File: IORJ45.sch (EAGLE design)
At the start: 19 parts, among them J3 RJ45-8X44UCON19514

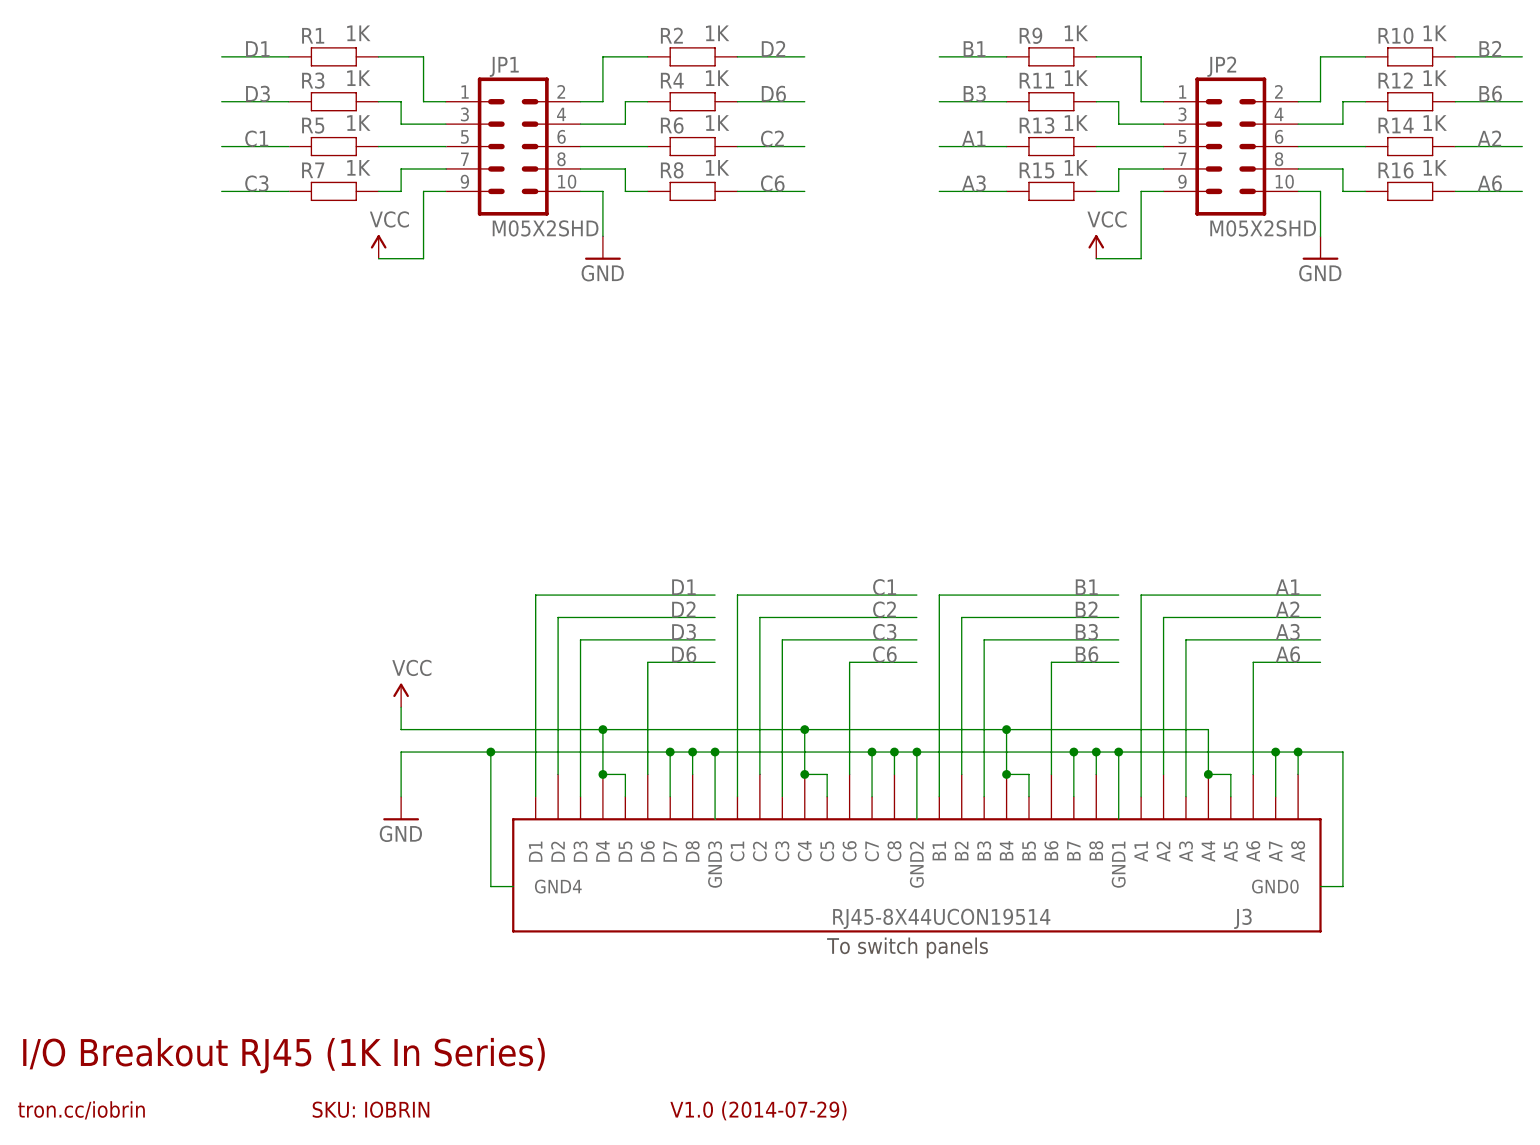
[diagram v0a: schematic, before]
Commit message: Converted to 2x6 header for v2.0 release
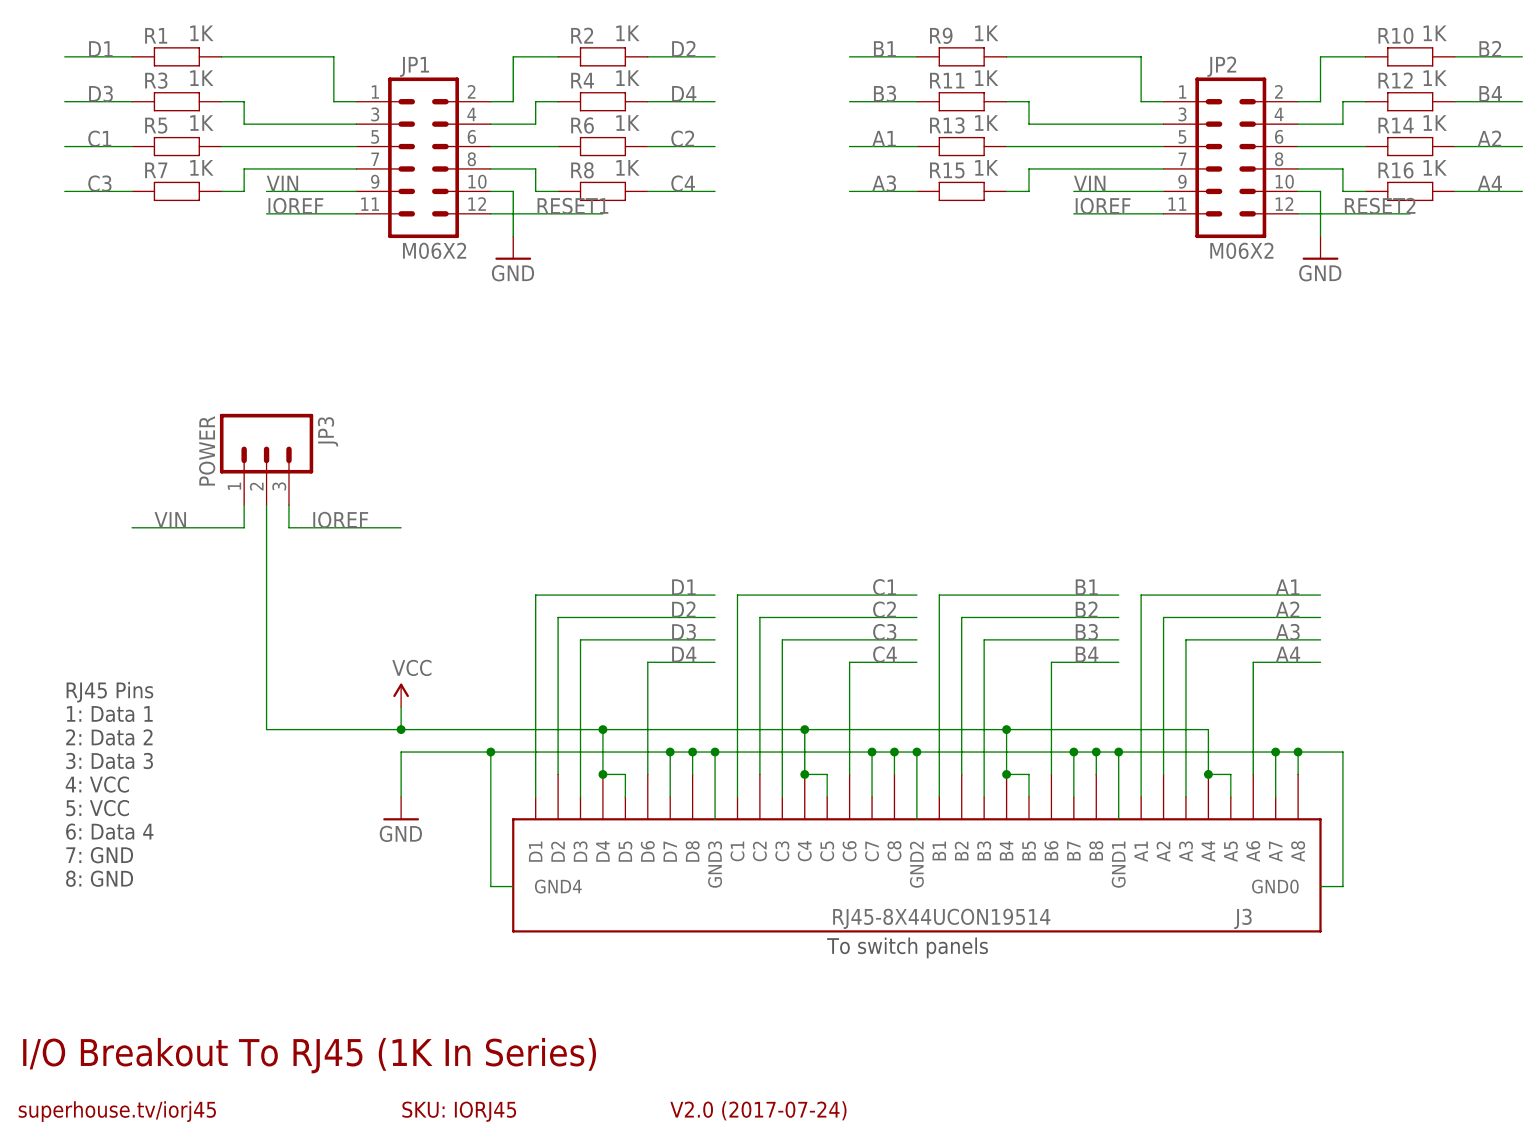
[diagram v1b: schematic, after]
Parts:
- added JP3: POWER, freetronics-jon:M03PTH
- J3: device freetronics-2:RJ45-8X44UCON19514 -> freetronics-jon:RJ45-8X44UCON19514
- JP1, JP2: value M05X2SHD -> M06X2; device freetronics-original:M05X2SHD -> freetronics-jon:M06X2
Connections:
- net A6 renamed A4
- net B6 renamed B4
- net C6 renamed C4
- net D6 renamed D4
- new net IOREF: JP1.11, JP2.11, JP3.3
- new net RESET1: JP1.12
- new net RESET2: JP2.12
- new net VIN: JP1.9, JP2.9, JP3.1
- net VCC: now also JP3.2; no longer JP1.9, JP2.9
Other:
- note added: "I/O Breakout To RJ45 (1K In Series)"
- note added: "RJ45 Pins 1: Data 1 2: Data 2 3: Data 3 4: VCC 5: VCC 6: Data 4 7: GND 8: GND"
- note added: "SKU: IORJ45"
- note added: "V2.0 (2017-07-24)"
- note added: "superhouse.tv/iorj45"
- note removed: "I/O Breakout RJ45 (1K In Series)"
- note removed: "SKU: IOBRIN"
- note removed: "V1.0 (2014-07-29)"
- note removed: "tron.cc/iobrin"
- moved on the sheet: R1, R11, R13, R15, R2, R3, R4, R5, R6, R7, R8, R9

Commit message: Part replacement using SuperHouse libraries
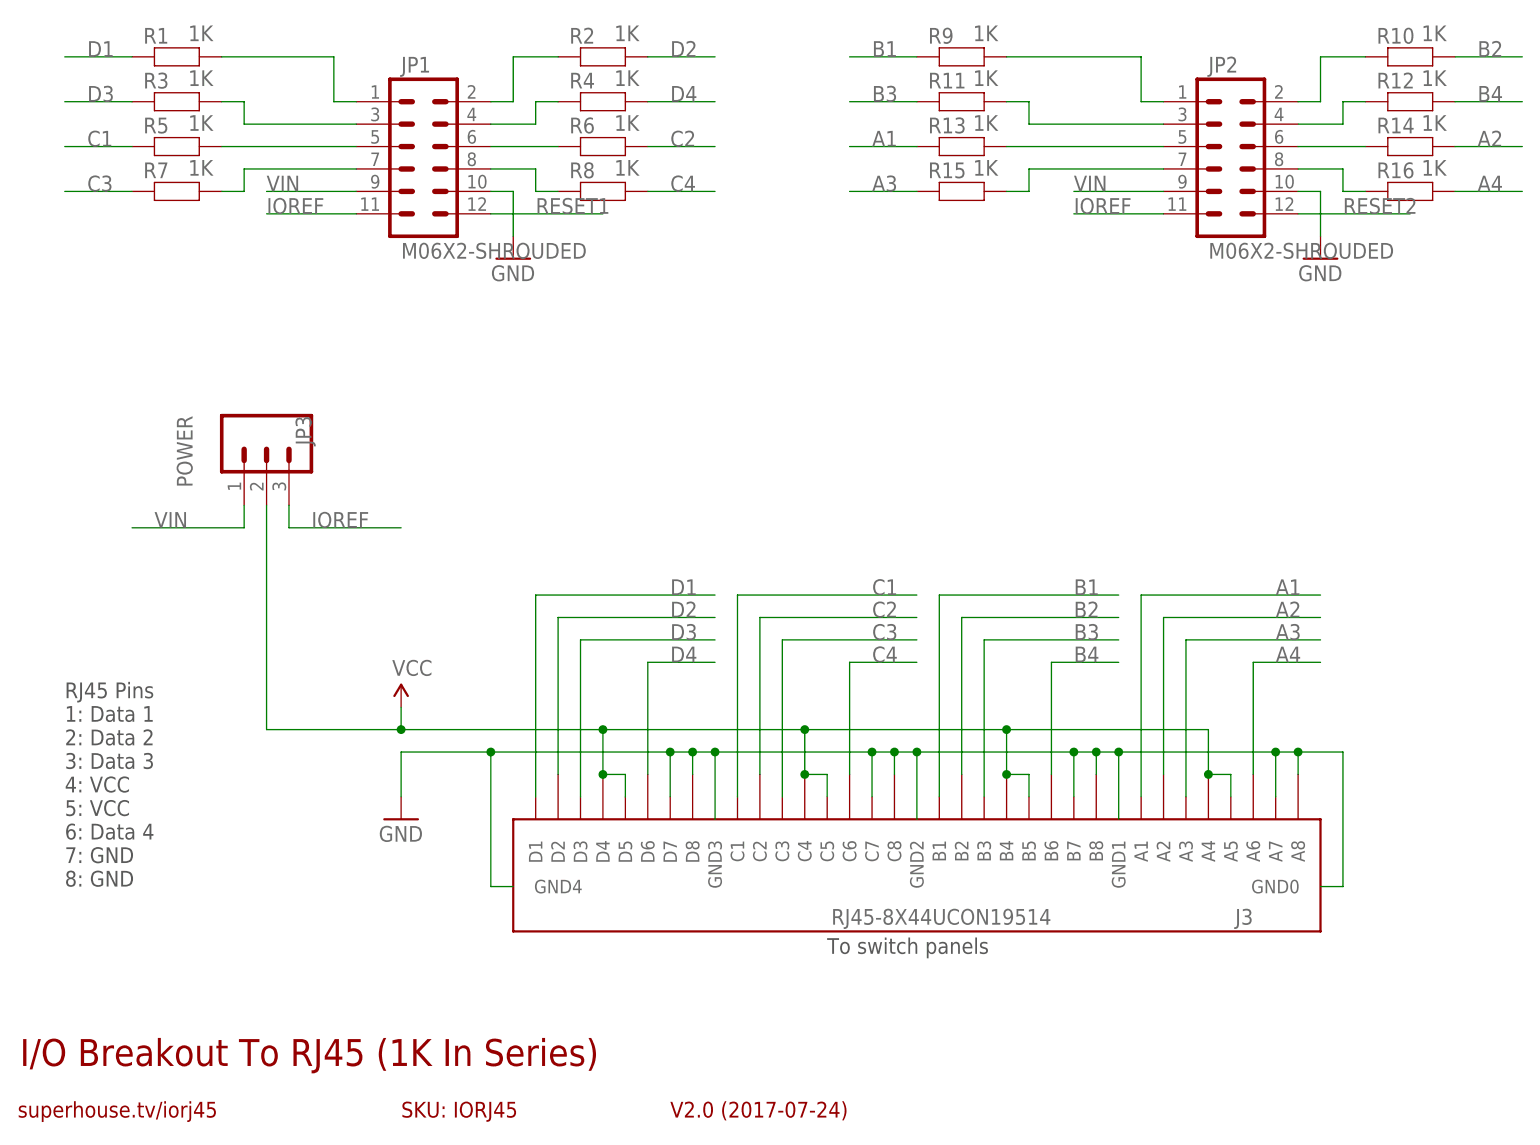
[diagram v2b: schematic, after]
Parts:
- J3: device freetronics-jon:RJ45-8X44UCON19514 -> SuperHouse-Connectors:RJ45-8X44UCON19514
- JP1, JP2: value M06X2 -> M06X2-SHROUDED; device freetronics-jon:M06X2 -> SuperHouse-Connectors:M06X2-SHROUDED
- JP3: device freetronics-jon:M03PTH -> SuperHouse-Connectors:M03-PIN
- R1, R10, R11, R12, R13, R14, R15, R16, R2, R3, R4, R5, R6, R7, R8, R9: device freetronics-jon:RESISTOR0603 -> SuperHouse-DiscreteSemi:RESISTOR0603
